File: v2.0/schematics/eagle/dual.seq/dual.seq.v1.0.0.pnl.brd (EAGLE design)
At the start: 74 x 22.9 mm, 13 parts, among them J1 CV3 OUT, J2 CV2 OUT, J3 CV1 OUT, J4 GATE3 OUT, J5 GATE2 OUT, J6 GATE1 OUT

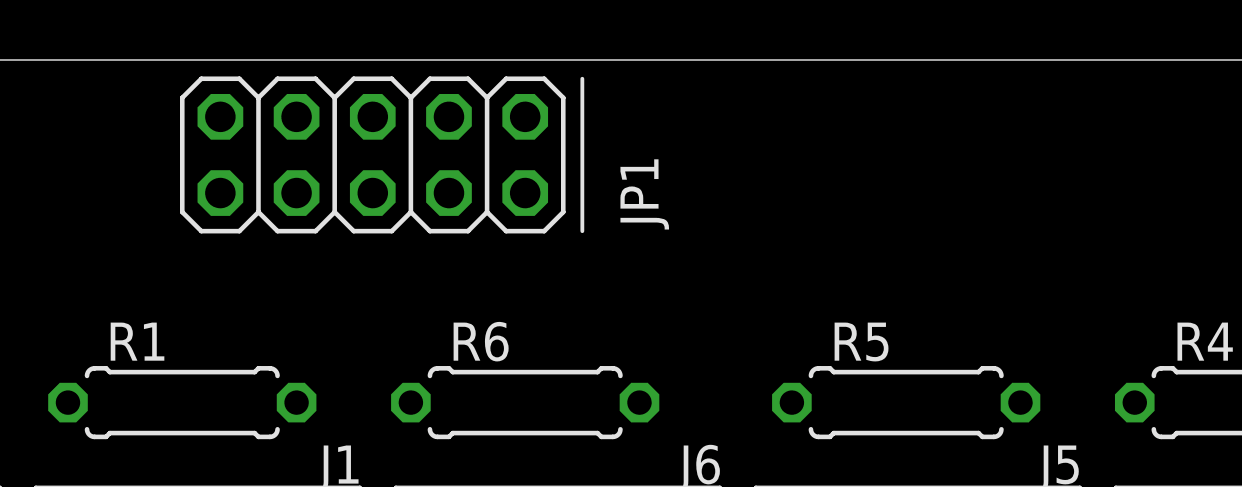
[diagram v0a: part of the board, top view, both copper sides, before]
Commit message: Inital routing for main pnl (too many vias)
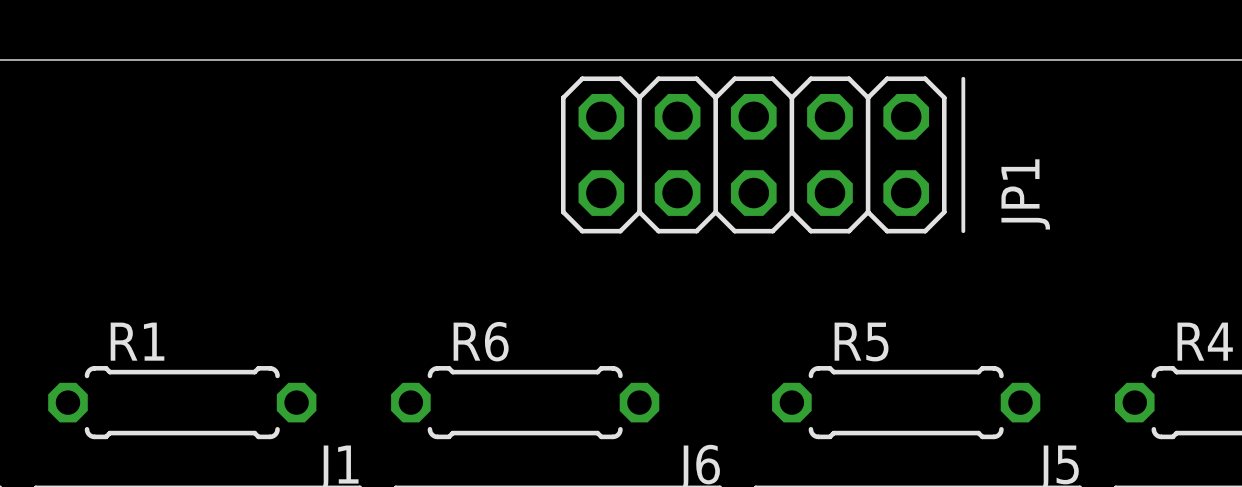
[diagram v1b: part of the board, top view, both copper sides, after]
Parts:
- moved JP1 12.7 mm to (49.5, 19.7)
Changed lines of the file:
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@@
 <element name="J5" library="jacks" package="CL1384" value="GATE2 OUT" x="59.7" y="2.4" rot="R180"/>
 <element name="J6" library="jacks" package="CL1384" value="GATE1 OUT" x="47.7" y="2.4" rot="R180"/>
-<element name="JP1" library="pinhead" package="2X05" value="TO MAIN" x="36.83" y="19.685" smashed="yes" rot="R180">
-<attribute name="NAME" x="45.085" y="19.685" size="1.27" layer="25" ratio="10" rot="R270"/>
-<attribute name="VALUE" x="43.18" y="16.51" size="1.27" layer="27" rot="R180"/>
+<element name="JP1" library="pinhead" package="2X05" value="TO MAIN" x="49.53" y="19.685" locked="yes" smashed="yes" rot="R180">
+<attribute name="NAME" x="57.785" y="19.685" size="1.27" layer="25" ratio="10" rot="R270"/>
+<attribute name="VALUE" x="55.88" y="16.51" size="1.27" layer="27" rot="R180"/>
 </element>
 <element name="R1" library="_common" package="0207/7" value="1K" x="30.48" y="11.43"/>
@@
 <wire x1="38.3" y1="2.4" x2="47.7" y2="2.4" width="0" layer="19" extent="1-1"/>
 <wire x1="14.3" y1="2.4" x2="38.3" y2="2.4" width="0" layer="19" extent="1-1"/>
-<wire x1="31.75" y1="20.955" x2="14.3" y2="2.4" width="0" layer="19" extent="1-1"/>
-<wire x1="31.75" y1="18.415" x2="31.75" y2="20.955" width="0" layer="19" extent="1-1"/>
+<wire x1="44.45" y1="20.955" x2="14.3" y2="2.4" width="0" layer="19" extent="1-1"/>
+<wire x1="44.45" y1="18.415" x2="44.45" y2="20.955" width="0" layer="19" extent="1-1"/>
 <wire x1="23.7" y1="2.4" x2="14.3" y2="2.4" width="0" layer="19" extent="1-1"/>
 <wire x1="2.3" y1="2.4" x2="23.7" y2="2.4" width="0" layer="19" extent="1-1"/>
-<wire x1="41.91" y1="20.955" x2="23.7" y2="2.4" width="0" layer="19" extent="1-1"/>
-<wire x1="41.91" y1="18.415" x2="41.91" y2="20.955" width="0" layer="19" extent="1-1"/>
+<wire x1="54.61" y1="20.955" x2="23.7" y2="2.4" width="0" layer="19" extent="1-1"/>
+<wire x1="54.61" y1="18.415" x2="54.61" y2="20.955" width="0" layer="19" extent="1-1"/>
 <wire x1="11.7" y1="2.4" x2="2.3" y2="2.4" width="0" layer="19" extent="1-1"/>
 </signal>
@@
 <contactref element="JP1" pad="3"/>
 <contactref element="R4" pad="2"/>
-<wire x1="39.37" y1="20.955" x2="69.85" y2="11.43" width="0" layer="19" extent="1-1"/>
+<wire x1="52.07" y1="20.955" x2="69.85" y2="11.43" width="0" layer="19" extent="1-1"/>
 </signal>
 <signal name="N$GATE2">
 <contactref element="JP1" pad="5"/>
 <contactref element="R5" pad="2"/>
-<wire x1="36.83" y1="20.955" x2="58.42" y2="11.43" width="0" layer="19" extent="1-1"/>
+<wire x1="49.53" y1="20.955" x2="58.42" y2="11.43" width="0" layer="19" extent="1-1"/>
 </signal>
 <signal name="N$GATE1">
 <contactref element="JP1" pad="7"/>
 <contactref element="R6" pad="1"/>
-<wire x1="34.29" y1="20.955" x2="38.1" y2="11.43" width="0" layer="19" extent="1-1"/>
+<wire x1="46.99" y1="20.955" x2="38.1" y2="11.43" width="0" layer="19" extent="1-1"/>
 </signal>
 <signal name="N$CV1">
 <contactref element="JP1" pad="8"/>
 <contactref element="R3" pad="1"/>
-<wire x1="3.81" y1="11.43" x2="34.29" y2="18.415" width="0" layer="19" extent="1-1"/>
+<wire x1="3.81" y1="11.43" x2="46.99" y2="18.415" width="0" layer="19" extent="1-1"/>
 </signal>
 <signal name="N$CV2">
 <contactref element="JP1" pad="6"/>
 <contactref element="R2" pad="1"/>
-<wire x1="36.83" y1="18.415" x2="15.24" y2="11.43" width="0" layer="19" extent="1-1"/>
+<wire x1="49.53" y1="18.415" x2="15.24" y2="11.43" width="0" layer="19" extent="1-1"/>
 </signal>
 <signal name="N$CV3">
 <contactref element="JP1" pad="4"/>
 <contactref element="R1" pad="1"/>
-<wire x1="26.67" y1="11.43" x2="39.37" y2="18.415" width="0" layer="19" extent="1-1"/>
+<wire x1="26.67" y1="11.43" x2="52.07" y2="18.415" width="0" layer="19" extent="1-1"/>
 </signal>
 <signal name="N$1">

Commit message: Route for dual.seq pnl
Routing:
- net 0V: track 0.00 -> 107.3 mm
- net N$CV1: track 0.00 -> 46.9 mm
- net N$CV2: track 0.00 -> 38.9 mm
- net N$CV3: track 0.00 -> 29.2 mm
- net N$GATE3: track 0.00 -> 21.7 mm
- net N$2: track 0.00 -> 15.2 mm
- net N$4: track 0.00 -> 15.0 mm
- net N$3: track 0.00 -> 14.8 mm
- net N$5: track 0.00 -> 14.5 mm
- net N$6: track 0.00 -> 14.4 mm
- net N$1: track 0.00 -> 14.3 mm
- net N$GATE1: track 0.00 -> 14.2 mm
- net N$GATE2: track 0.00 -> 13.8 mm
